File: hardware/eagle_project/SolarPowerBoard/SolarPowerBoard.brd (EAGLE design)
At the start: 68.8 x 53.6 mm, 82 parts, among them IC1 BQ29700DSET_BQ29700DSET, IC3 TPS63031DSKT_TPS63031DSKT, J2 105017-0001_105017-0001, J5 XG8S-0331_XG8S-0331, K1 G6E-134P-US_DC5_G6E-134P-US_D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, Q3 DAVIDE_FDN302P, U4 MCP73831T-2ACI_OT_MCP73831T-2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

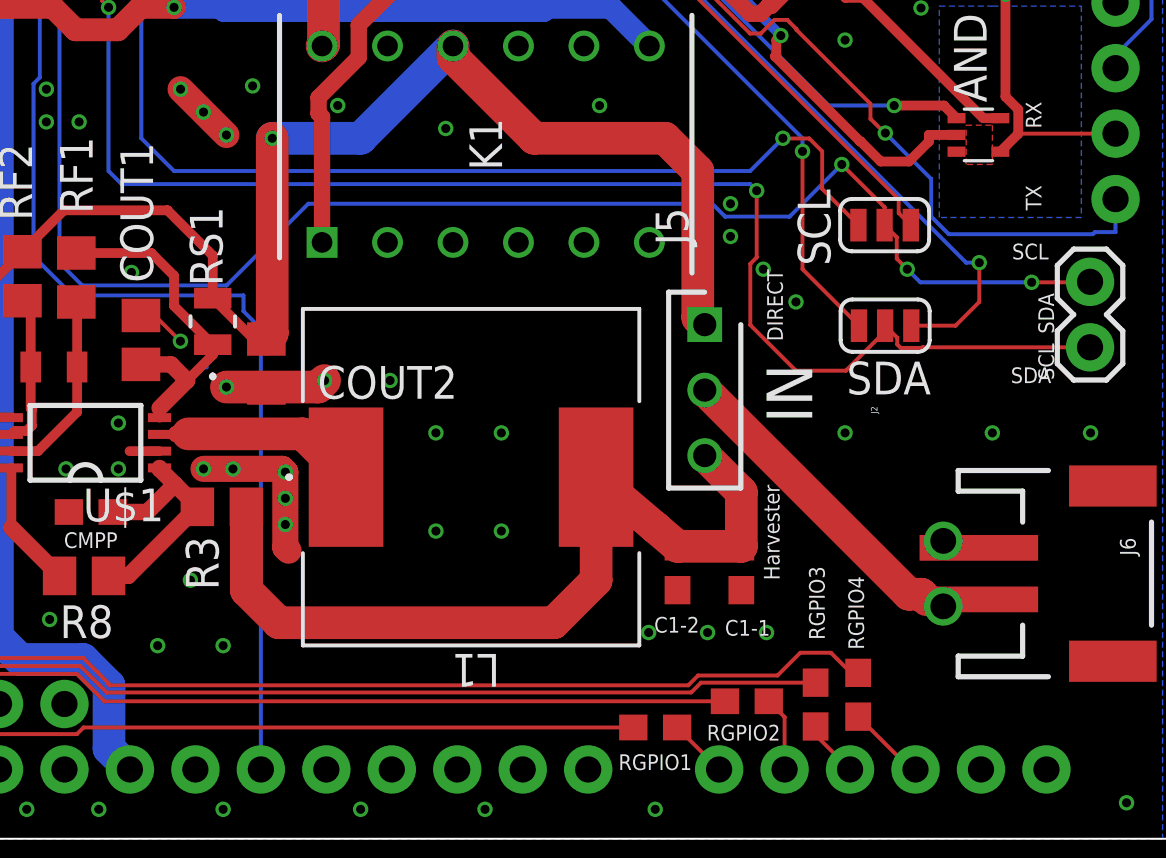
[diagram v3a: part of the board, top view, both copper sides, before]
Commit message: Changed inductor footprint
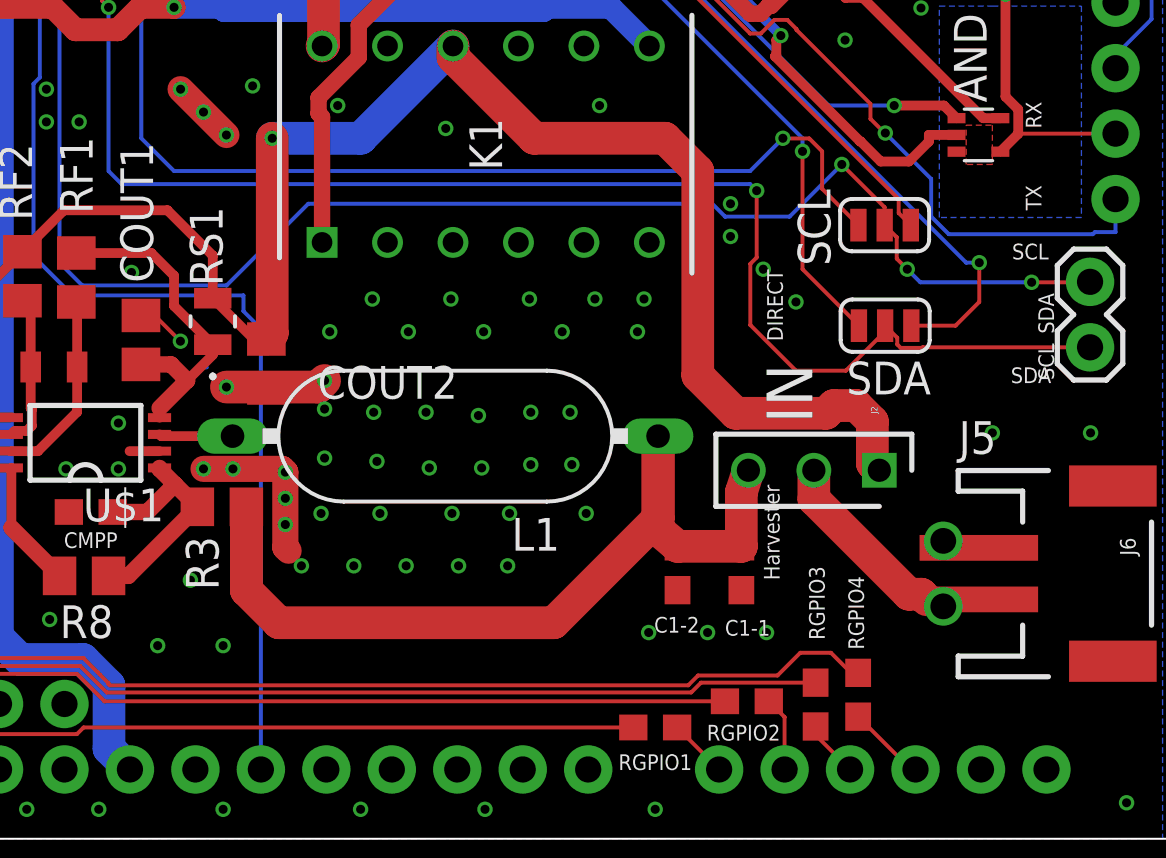
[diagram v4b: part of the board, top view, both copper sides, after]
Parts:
- L1: value SOLARPOWERBOARD_SRR1280-270M -> EMC9714; device SolarPowerBoard:SOLARPOWERBOARD_IND_BOURNS_SRR1280 -> inductors:EMC9714
- moved J5 8.82 mm to (56.6, 13.8), turned to 180 degrees
- moved L1 1.88 mm to (39.7, 15.1), turned to 180 degrees
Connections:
- net N$1: now also L1.1; no longer L1.2
- net N$18: now also L1.2; no longer L1.1
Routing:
- net SOLAR_OUTPUT: track 50.3 -> 61.9 mm
- net N$16: track 13.5 -> 8.62 mm
- net N$18: track 7.29 -> 2.86 mm
- net N$1: track 32.7 -> 34.8 mm
- net GND: vias 130 -> 156

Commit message: Changed sense resistor
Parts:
- R10: value (none) -> 330
- R9: value (none) -> 2.2k
- RCG3: value (none) -> KRL2012E-C-R020-F; device SolarPowerBoard:SPARKFUN-RESISTORS_0805:2 -> SolarPowerBoard:RESC1216X70N
- moved RCG3 0.29 mm to (15.4, 32.3)
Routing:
- net POWER_INPUT: track 50.5 -> 49.4 mm
- net PACK+: track 44.3 -> 43.5 mm
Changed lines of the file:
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@@
 <attribute name="OC_NEWARK" value="08N2144" x="-56.566" y="-1.392" size="1.778" layer="27" rot="R270" display="off"/>
 </element>
-<element name="R10" library="SolarPowerBoard" package="SPARKFUN-RESISTORS_0805:2" value=" " x="13.261" y="33.567" rot="R270">
+<element name="R10" library="SolarPowerBoard" package="SPARKFUN-RESISTORS_0805:2" value="330" x="13.261" y="33.567" rot="R270">
 <attribute name="MF" value="" x="-74.369" y="-31.203" size="1.778" layer="27" rot="R270" display="off"/>
 <attribute name="MPN" value="ERJ-6GEYJ331V" x="-74.369" y="-31.203" size="1.778" layer="27" rot="R270" display="off"/>
@@
 <attribute name="OC_NEWARK" value="79M6013" x="-6.031" y="87.162" size="1.778" layer="27" rot="R180" display="off"/>
 </element>
-<element name="R9" library="SolarPowerBoard" package="SPARKFUN-RESISTORS_0805:2" value=" " x="12.456" y="13.108">
+<element name="R9" library="SolarPowerBoard" package="SPARKFUN-RESISTORS_0805:2" value="2.2k" x="12.456" y="13.108">
 <attribute name="MF" value="" x="73.416" y="-74.522" size="1.778" layer="27" display="off"/>
 <attribute name="MPN" value="CR0805-FX-2201ELF" x="73.416" y="-74.522" size="1.778" layer="27" display="off"/>
@@
 <attribute name="MPN" value="LAUNCHXL-CC2650" x="-60.2582" y="49.8062" size="1.778" layer="27" rot="R180" display="off"/>
 <attribute name="OC_NEWARK" value="82Y0957" x="-60.2582" y="49.8062" size="1.778" layer="27" rot="R180" display="off"/>
-</element>
-<element name="RCG3" library="SolarPowerBoard" package="SPARKFUN-RESISTORS_0805:2" value=" " x="15.634" y="32.223" rot="R180">
-<attribute name="MF" value="" x="-73.266" y="114.773" size="1.778" layer="27" rot="R180" display="off"/>
-<attribute name="MPN" value="" x="-73.266" y="114.773" size="1.778" layer="27" rot="R180" display="off"/>
-<attribute name="NAME" x="15.634" y="31.334" size="0.6096" layer="25" font="vector" ratio="20" rot="R180" align="bottom-center"/>
-<attribute name="OC_NEWARK" value="unknown" x="-73.266" y="114.773" size="1.778" layer="27" rot="R180" display="off"/>
-<attribute name="PROD_ID" value=" " x="-73.266" y="114.773" size="1.778" layer="27" rot="R180" display="off"/>
 </element>
 <element name="RF1" library="SolarPowerBoard" package="RESISTOR_R0805" value="1k" x="25.4186" y="21.2681" rot="R90">
@@
 <attribute name="SPICEPREFIX" value="L" x="39.734" y="15.114" size="1.778" layer="27" rot="R180" display="off"/>
 <attribute name="VALUE" x="44.814" y="15.749" size="1.27" layer="27" ratio="10" rot="R180"/>
+</element>
+<element name="RCG3" library="SolarPowerBoard" package="RESC1216X70N" value="KRL2012E-C-R020-F" x="15.351" y="32.258" rot="R180">
+<attribute name="ARROW_PART_NUMBER" value="KRL2012E-C-R020-F" x="15.351" y="32.258" size="1.778" layer="27" rot="R180" display="off"/>
+<attribute name="ARROW_PRICE-STOCK" value="http://uk.rs-online.com/web/p/products/1346103" x="15.351" y="32.258" size="1.778" layer="27" rot="R180" display="off"/>
+<attribute name="DESCRIPTION" value="Susumu Co KRL Series Metal Foil Surface Mount Fixed Resistor 2012 Case 20m 1% 1W 50ppm/C" x="15.351" y="32.258" size="1.778" layer="27" rot="R180" display="off"/>
+<attribute name="HEIGHT" value="0.7mm" x="15.351" y="32.258" size="1.778" layer="27" rot="R180" display="off"/>
+<attribute name="MANUFACTURER_NAME" value="Susumu" x="15.351" y="32.258" size="1.778" layer="27" rot="R180" display="off"/>
+<attribute name="MANUFACTURER_PART_NUMBER" value="KRL2012E-C-R020-F" x="15.351" y="32.258" size="1.778" layer="27" rot="R180" display="off"/>
+<attribute name="NAME" x="21.351" y="31.258" size="1.27" layer="25" rot="R180" align="center"/>
+<attribute name="RS_PART_NUMBER" value="1346103" x="15.351" y="32.258" size="1.778" layer="27" rot="R180" display="off"/>
+<attribute name="RS_PRICE-STOCK" value="http://uk.rs-online.com/web/p/products/1346103" x="15.351" y="32.258" size="1.778" layer="27" rot="R180" display="off"/>
+<attribute name="VALUE" x="17.351" y="35.258" size="1.27" layer="27" rot="R180" align="center"/>
 </element>
 </elements>
@@
 <contactref element="U$3" pad="7"/>
 <contactref element="U$3" pad="6"/>
-<contactref element="RCG3" pad="2"/>
 <contactref element="C7" pad="2"/>
 <contactref element="JP1" pad="3"/>
@@
 <wire x1="10.574" y1="31.91" x2="11.331" y2="32.667" width="1.27" layer="1"/>
 <wire x1="13.261" y1="32.667" x2="14.29" y2="32.667" width="1.27" layer="1"/>
-<wire x1="14.29" y1="32.667" x2="14.734" y2="32.223" width="1.27" layer="1"/>
 <wire x1="16.872" y1="40.36" x2="16.663" y2="40.36" width="0.1524" layer="1"/>
 <wire x1="16.663" y1="40.36" x2="16.129" y2="40.894" width="0.1524" layer="1"/>
@@
 <wire x1="15.113" y1="33.655" x2="15.24" y2="33.528" width="0.1524" layer="16"/>
 <via x="15.24" y="33.528" extent="1-16" drill="0.35"/>
-<wire x1="15.24" y1="33.528" x2="15.367" y2="33.401" width="0.1524" layer="1"/>
-<wire x1="15.367" y1="33.401" x2="15.367" y2="32.766" width="0.1524" layer="1"/>
-<wire x1="15.367" y1="32.766" x2="14.824" y2="32.223" width="0.1524" layer="1"/>
-<wire x1="14.824" y1="32.223" x2="14.734" y2="32.223" width="0.1524" layer="1"/>
 <wire x1="16.129" y1="40.894" x2="12.51239375" y2="40.894" width="0.1524" layer="1"/>
 <wire x1="12.479196875" y1="40.860803125" x2="11.523803125" y2="40.860803125" width="0.1524" layer="1"/>
@@
 <wire x1="20.066" y1="35.56" x2="18.796" y2="34.29" width="0.1524" layer="1"/>
 <wire x1="18.956" y1="39.78" x2="19.464" y2="39.78" width="0.1524" layer="1"/>
+<contactref element="RCG3" pad="2"/>
+<wire x1="15.24" y1="33.528" x2="14.859" y2="33.147" width="0.1524" layer="1"/>
+<wire x1="14.859" y1="33.147" x2="14.859" y2="32.366" width="0.1524" layer="1"/>
+<wire x1="14.859" y1="32.366" x2="14.751" y2="32.258" width="0.1524" layer="1"/>
 <wire x1="16.872" y1="40.36" x2="16.872" y2="39.96" width="0" layer="19" extent="1-1"/>
+<wire x1="12.4598" y1="35.64760625" x2="12.4392" y2="35.87399375" width="0" layer="19" extent="1-16"/>
 <wire x1="9.93" y1="32.18" x2="10.574" y2="31.91" width="0" layer="19" extent="1-1"/>
 </signal>
@@
 <contactref element="K1" pad="7"/>
 <contactref element="U$3" pad="10"/>
-<contactref element="RCG3" pad="1"/>
 <contactref element="C2" pad="1"/>
 <contactref element="IC3" pad="5"/>
 <wire x1="28.46" y1="33.93" x2="28.46" y2="34.83645" width="1.27" layer="1"/>
-<wire x1="16.534" y1="32.223" x2="16.037" y2="32.223" width="0.1524" layer="1"/>
-<wire x1="15.748" y1="33.655" x2="15.8818" y2="33.7888" width="0.1524" layer="1"/>
-<wire x1="16.037" y1="32.223" x2="15.748" y2="32.512" width="0.1524" layer="1"/>
-<wire x1="15.748" y1="32.512" x2="15.748" y2="33.655" width="0.1524" layer="1"/>
+<wire x1="15.748" y1="32.512" x2="16.037" y2="32.223" width="0.1524" layer="1"/>
 <wire x1="12.065" y1="39.37" x2="12.0674" y2="39.37" width="0.1524" layer="16"/>
 <wire x1="12.0674" y1="39.37" x2="12.192" y2="39.4946" width="0.1524" layer="16"/>
@@
 <wire x1="12.192" y1="39.4946" x2="13.8066" y2="39.4946" width="0.1524" layer="1"/>
 <wire x1="13.8066" y1="39.4946" x2="13.872" y2="39.56" width="0.1524" layer="1"/>
-<wire x1="15.8818" y1="33.7888" x2="15.70420625" y2="33.96639375" width="0.1524" layer="1"/>
-<wire x1="15.70420625" y1="33.96639375" x2="15.70420625" y2="34.65120625" width="0.1524" layer="1"/>
+<wire x1="15.70420625" y1="33.96639375" x2="15.70420625" y2="34" width="0.1524" layer="1"/>
+<wire x1="15.70420625" y1="34" x2="15.70420625" y2="34.65120625" width="0.1524" layer="1"/>
 <wire x1="15.70420625" y1="34.65120625" x2="15.3102125" y2="35.0452" width="0.1524" layer="1"/>
 <wire x1="15.3102125" y1="35.0452" x2="14.351" y2="35.0452" width="0.1524" layer="1"/>
@@
 <wire x1="25.38490625" y1="30.8805" x2="24.51540625" y2="31.75" width="0.889" layer="1"/>
 <wire x1="16.51" y1="31.75" x2="16.534" y2="31.774" width="0.1524" layer="1"/>
-<wire x1="16.534" y1="31.774" x2="16.534" y2="32.223" width="0.1524" layer="1"/>
 <wire x1="28.46" y1="33.93" x2="28.46" y2="35.4" width="0.1524" layer="1"/>
+<contactref element="RCG3" pad="1"/>
+<wire x1="15.70420625" y1="34" x2="15.748" y2="33.95620625" width="0.1524" layer="1"/>
+<wire x1="15.748" y1="33.95620625" x2="15.748" y2="32.512" width="0.1524" layer="1"/>
+<wire x1="16.037" y1="32.223" x2="16.51" y2="31.75" width="0" layer="19" extent="1-1"/>
+<wire x1="15.951" y1="32.258" x2="16.037" y2="32.223" width="0" layer="19" extent="1-1"/>
 </signal>
 <signal name="SOLAR_OUTPUT">

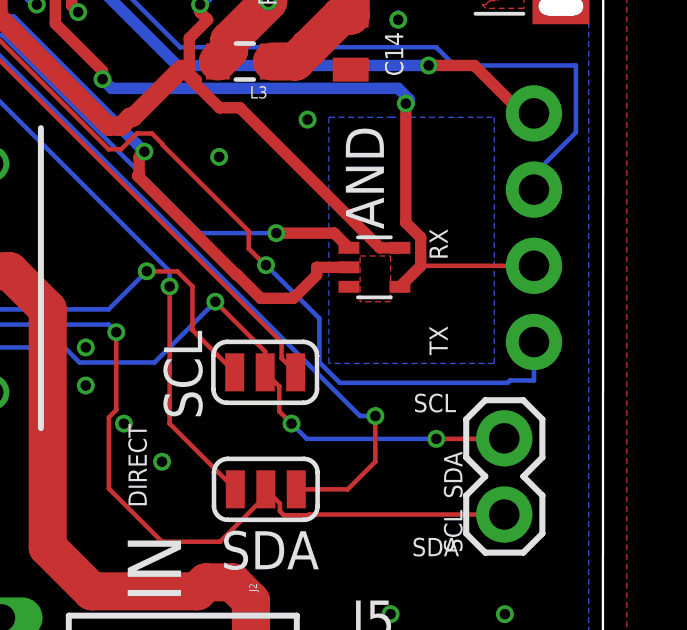
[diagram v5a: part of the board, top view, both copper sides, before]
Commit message: Added 0ohm resistor between UART AND port and RX pin. Removed library autosave files.
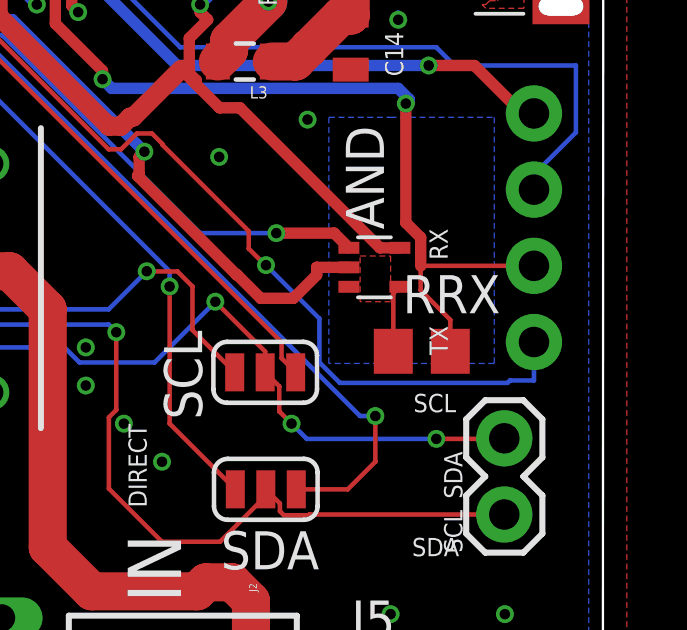
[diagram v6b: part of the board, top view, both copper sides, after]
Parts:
- added RRX: 0, resistor:R0805
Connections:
- net DP5_UART_FTDI_RX: now also RRX.1, RRX.2
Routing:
- net DP5_UART_FTDI_RX: track 26.0 -> 30.5 mm
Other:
- board text added: "BATT"
- board text added: "SOLAR"
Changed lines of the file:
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@@
 <text x="31.623" y="40.894" size="0.4064" layer="25">USB-CHARGING</text>
 <rectangle x1="18.2897" y1="38.021" x2="39.6892" y2="41.8215" layer="40"/>
+<text x="59.055" y="3.429" size="1.778" layer="51">SOLAR</text>
+<text x="-0.127" y="24.511" size="1.778" layer="51">BATT</text>
 </plain>
 <attributes>
@@
 <attribute name="RS_PRICE-STOCK" value="http://uk.rs-online.com/web/p/products/1346103" x="15.351" y="32.258" size="1.778" layer="27" rot="R180" display="off"/>
 <attribute name="VALUE" x="17.351" y="35.258" size="1.27" layer="27" rot="R180" align="center"/>
+</element>
+<element name="RRX" library="resistor" library_urn="urn:adsk.eagle:library:348" package="R0805" package3d_urn="urn:adsk.eagle:package:23553/2" value="0" x="62" y="24">
+<attribute name="NAME" x="61.365" y="25.27" size="1.27" layer="25"/>
+<attribute name="VALUE" x="61.365" y="21.46" size="1.27" layer="27"/>
 </element>
 </elements>
@@
 </signal>
 <signal name="DP5_UART_FTDI_RX">
-<contactref element="AND" pad="4"/>
 <contactref element="FT230XQ-R" pad="2"/>
 <contactref element="RX_TX" pad="2"/>
@@
 <wire x1="61.468" y1="28.28693125" x2="61.9629" y2="27.79203125" width="0.381" layer="1"/>
 <wire x1="61.9629" y1="27.79203125" x2="61.9629" y2="26.8429" width="0.381" layer="1"/>
-<wire x1="61.9629" y1="26.8429" x2="61.27" y2="26.15" width="0.381" layer="1"/>
 <wire x1="61.9629" y1="26.8429" x2="61.97" y2="26.85" width="0.1524" layer="1"/>
 <wire x1="65.739" y1="26.85" x2="61.97" y2="26.85" width="0.1524" layer="1"/>
@@
 <wire x1="49.8158" y1="36.938" x2="49.784" y2="36.9062" width="0.381" layer="1"/>
 <wire x1="51.66194375" y1="32.766" x2="61.214" y2="32.766" width="0.381" layer="16"/>
+<contactref element="AND" pad="4"/>
+<contactref element="RRX" pad="1"/>
+<contactref element="RRX" pad="2"/>
+<wire x1="61.27" y1="26.15" x2="61.05" y2="25.93" width="0.1524" layer="1"/>
+<wire x1="61.05" y1="25.93" x2="61.05" y2="24" width="0.1524" layer="1"/>
+<wire x1="62.95" y1="24" x2="62.95" y2="25.05" width="0.1524" layer="1"/>
+<wire x1="61.9629" y1="26.0371" x2="61.9629" y2="26.8429" width="0.1524" layer="1"/>
+<wire x1="62.95" y1="25.05" x2="61.9629" y2="26.0371" width="0.1524" layer="1"/>
+<wire x1="61.9629" y1="26.0371" x2="61.27" y2="26.15" width="0" layer="19" extent="1-1"/>
 </signal>
 <signal name="N$25">
